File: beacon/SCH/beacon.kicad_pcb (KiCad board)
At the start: 2 copper layers, 38.4 x 28.2 mm, 10 parts, among them P1 CONNECTOR, U1 74LS14, U2 LM555N, U3 QFM-TX1

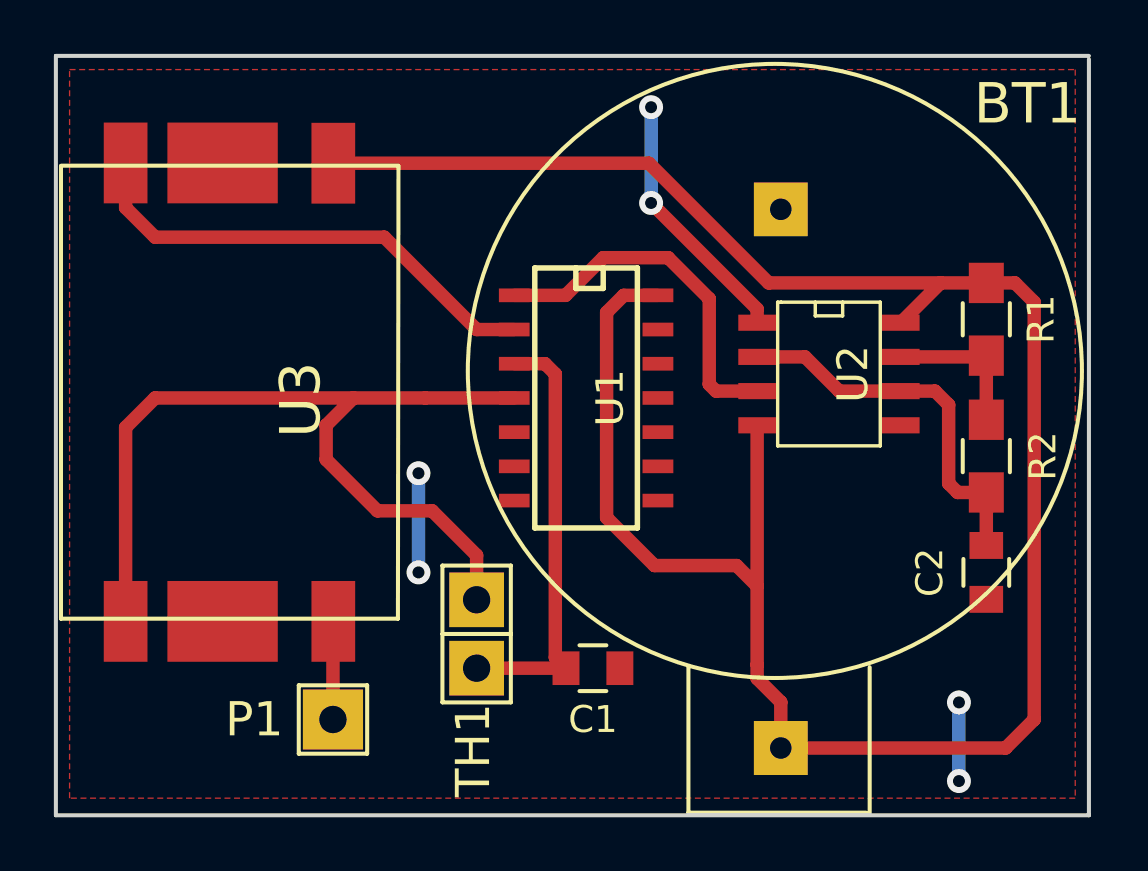
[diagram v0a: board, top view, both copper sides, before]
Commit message: jumpers reduced
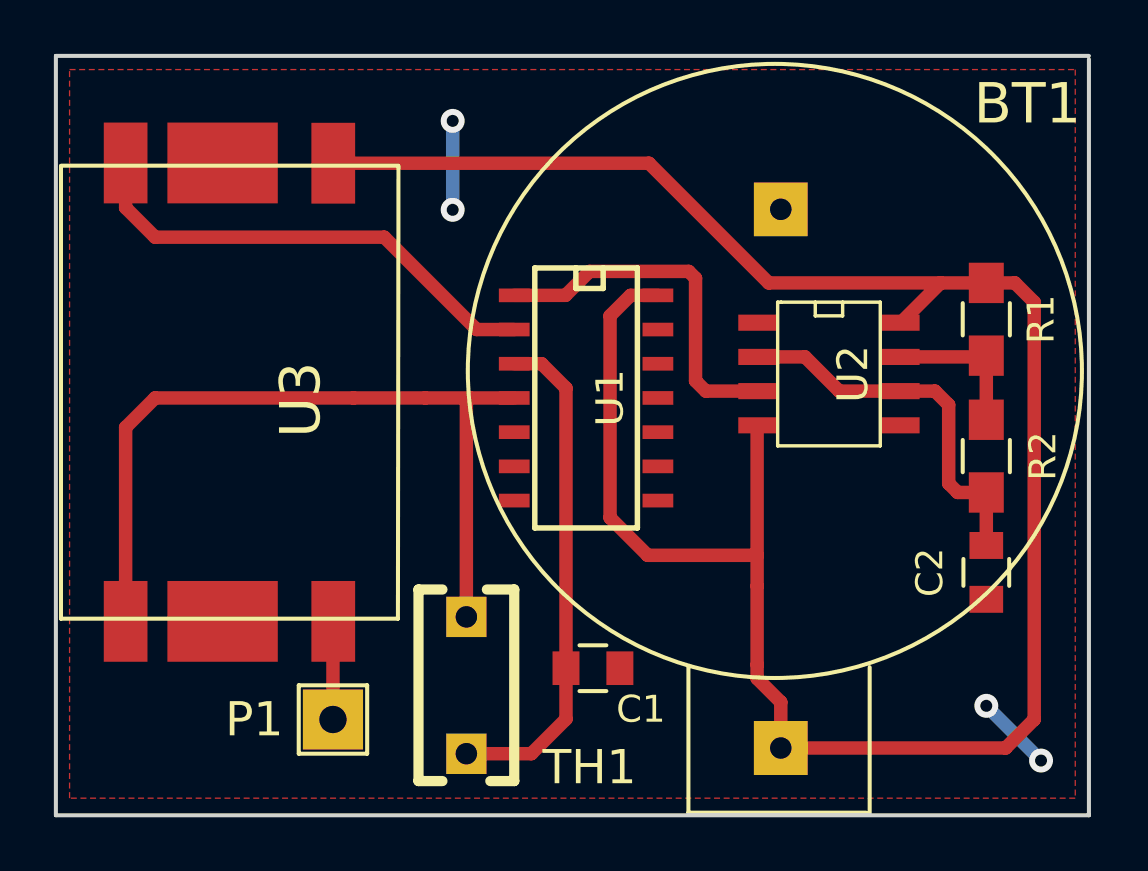
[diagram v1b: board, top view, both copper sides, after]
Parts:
- TH1: footprint Pin_Headers:Pin_Header_Straight_1x02 -> Capacitors_ThroughHole:Capacitor7x3-5RM5_RevB
- moved TH1 1.94 mm to (137.3, 117.5)
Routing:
- net GND: track 16.4 -> 6.18 mm, vias 6 -> 4
- net DATA: track 33.5 -> 30.3 mm
- net Net-(C1-Pad2): track 16.5 -> 18.8 mm
- net VCC: track 84.4 -> 83.6 mm

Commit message: last improvments and pcbs
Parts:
- added C3: 100nF, Capacitors_SMD:C_0805, F.Cu at (149.4, 111.0)
- added C4: 100nF, Capacitors_SMD:C_0805, F.Cu at (137.9, 98.0)
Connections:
- U1 pad 11: (no net) -> GND
- U1 pad 13: (no net) -> GND
- U1 pad 5: (no net) -> GND
- U1 pad 9: (no net) -> GND
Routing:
- net GND: track 6.18 -> 23.2 mm
- net VCC: track 83.6 -> 75.7 mm
- net ENABLE: track 18.0 -> 19.3 mm
- net Net-(U1-Pad1): track 13.5 -> 12.8 mm
